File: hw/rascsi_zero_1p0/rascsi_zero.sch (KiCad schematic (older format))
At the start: 89 parts, among them IC1 SN74LS641-1DW, IC2 SN74LS641-1DW, IC3 SN74LS641-1DW, IC4 SN74LS641-1DW, J1 Raspberry_Pi_2_3, J2 DNP, J3 U254-051N-4BH806, J4 I2C Pinout, J6 CONNFLY DB-25, J7 DNP, X2 Dogcow, X4 Dogcow, X5 Dogcow, X6 Dogcow, X7 Pi

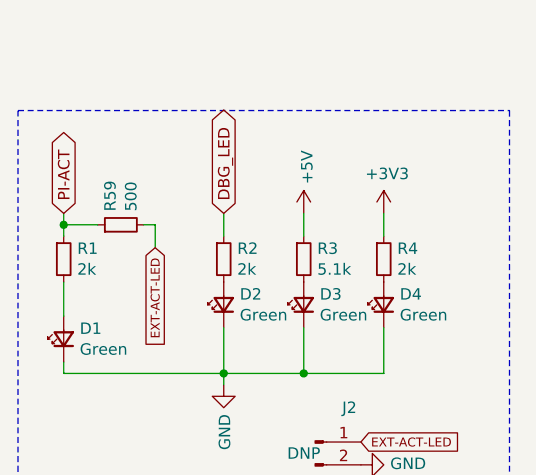
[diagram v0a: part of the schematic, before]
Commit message: Alternate resistor part, since 500 ohm is out of stock
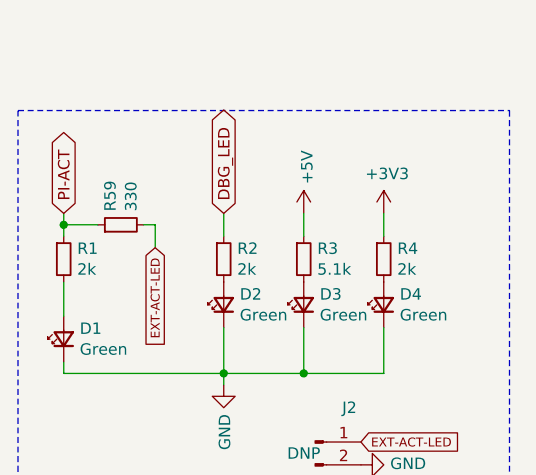
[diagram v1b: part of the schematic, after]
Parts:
- R59: value 500 -> 330; LCSC C17408 -> C17630
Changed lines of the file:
@@
 P 1000 1050
 F 0 "R59" H 1059 1096 50  0000 L CNN
-F 1 "500" H 1059 1005 50  0000 L CNN
+F 1 "330" H 1059 1005 50  0000 L CNN
 F 2 "Resistor_SMD:R_0805_2012Metric" H 1000 1050 50  0001 C CNN
 F 3 "" H 1000 1050 50  0001 C CNN
-F 4 "C17408" H 1000 1050 50  0001 C CNN "LCSC"
+F 4 "C17630" H 1000 1050 50  0001 C CNN "LCSC"
 	1    1000 1050
 	0    -1   -1   0
